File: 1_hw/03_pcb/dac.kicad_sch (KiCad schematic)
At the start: 6 parts, among them U16 AD9850, U17 AD9744

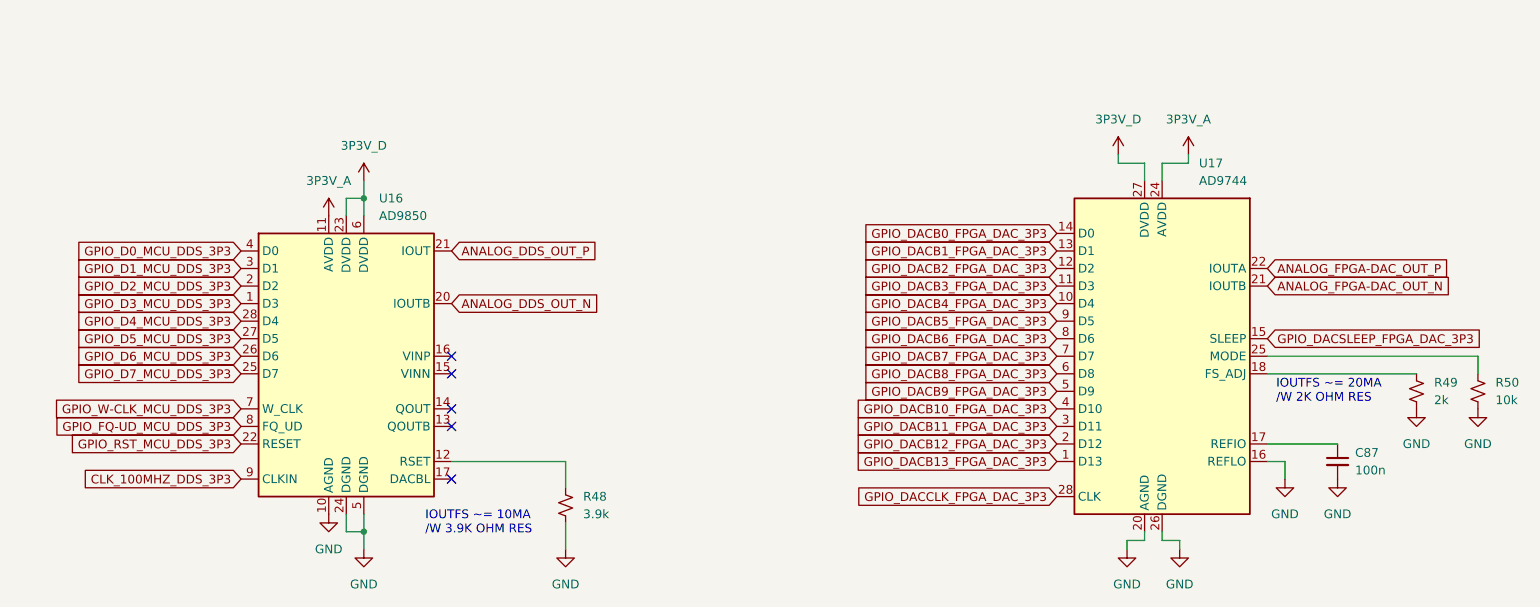
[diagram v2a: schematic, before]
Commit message: FEAT: Added MCU Flash. Finished creating & assigning footprints. Ran ERC & cleared out issues. Ready for Layout.
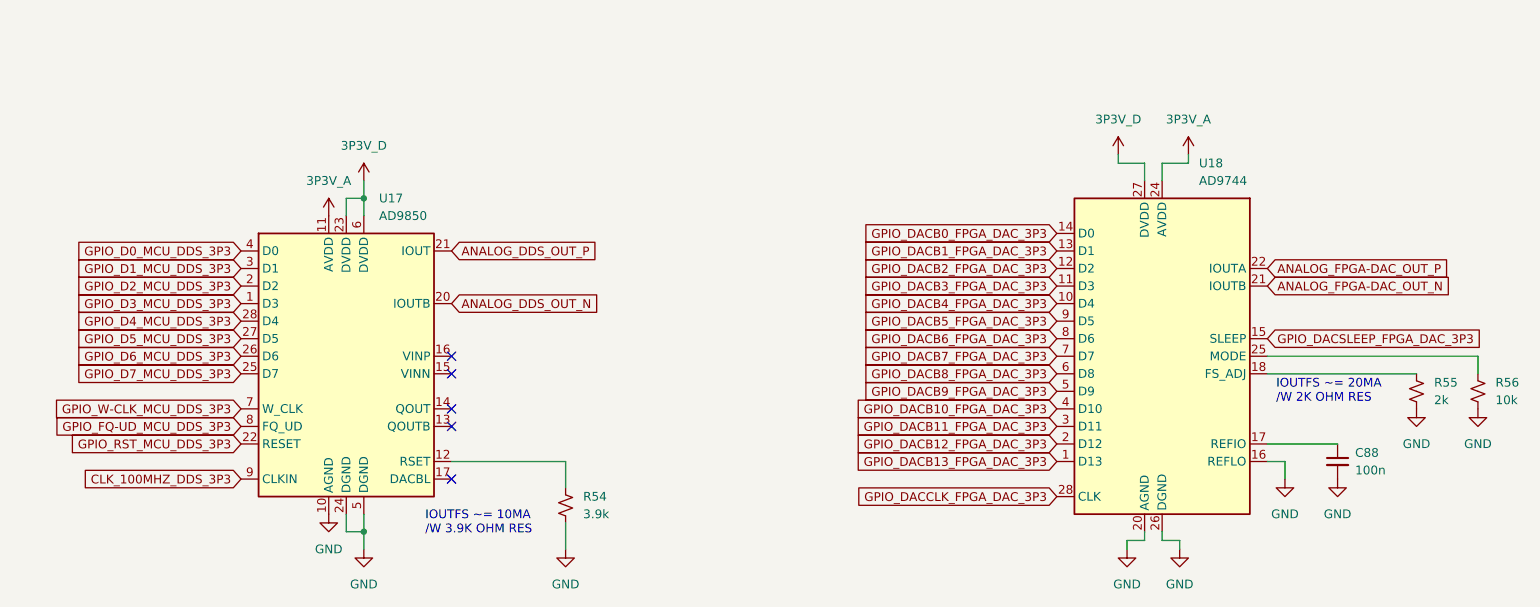
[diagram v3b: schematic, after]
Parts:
- renumbered C87 to C88, R48 to R54, R49 to R55, R50 to R56, U16 to U17, U17 to U18
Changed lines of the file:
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@@
 		(dnp no)
 		(fields_autoplaced yes)
-		(property "Reference" "#PWR0202"
+		(property "Reference" "#PWR0217"
 			(at 204.47 120.65 0)
 			(effects
@@
 			(project "arb"
 				(path "/866ef9be-3b01-4288-a6e0-a2357aa17e50/7126ceca-2dec-4994-855f-f217c0acdc71"
-					(reference "#PWR0202")
+					(reference "#PWR0217")
 					(unit 1)
 				)
@@
 		(dnp no)
 		(fields_autoplaced yes)
-		(property "Reference" "#PWR0206"
+		(property "Reference" "#PWR0221"
 			(at 234.95 110.49 0)
 			(effects
@@
 			(project "arb"
 				(path "/866ef9be-3b01-4288-a6e0-a2357aa17e50/7126ceca-2dec-4994-855f-f217c0acdc71"
-					(reference "#PWR0206")
+					(reference "#PWR0221")
 					(unit 1)
 				)
@@
 		(dnp no)
 		(fields_autoplaced yes)
-		(property "Reference" "#PWR0203"
+		(property "Reference" "#PWR0218"
 			(at 212.09 120.65 0)
 			(effects
@@
 			(project "arb"
 				(path "/866ef9be-3b01-4288-a6e0-a2357aa17e50/7126ceca-2dec-4994-855f-f217c0acdc71"
-					(reference "#PWR0203")
+					(reference "#PWR0218")
 					(unit 1)
 				)
@@
 		(dnp no)
 		(fields_autoplaced yes)
-		(property "Reference" "U16"
+		(property "Reference" "U17"
 			(at 96.1741 63.5 0)
 			(effects
@@
 			(project ""
 				(path "/866ef9be-3b01-4288-a6e0-a2357aa17e50/7126ceca-2dec-4994-855f-f217c0acdc71"
-					(reference "U16")
+					(reference "U17")
 					(unit 1)
 				)
@@
 		(dnp no)
 		(fields_autoplaced yes)
-		(property "Reference" "#PWR0198"
+		(property "Reference" "#PWR0213"
 			(at 93.98 64.77 0)
 			(effects
@@
 			(project "arb"
 				(path "/866ef9be-3b01-4288-a6e0-a2357aa17e50/7126ceca-2dec-4994-855f-f217c0acdc71"
-					(reference "#PWR0198")
+					(reference "#PWR0213")
 					(unit 1)
 				)
@@
 		(dnp no)
 		(fields_autoplaced yes)
-		(property "Reference" "#PWR0200"
+		(property "Reference" "#PWR0215"
 			(at 123.19 120.65 0)
 			(effects
@@
 			(project "arb"
 				(path "/866ef9be-3b01-4288-a6e0-a2357aa17e50/7126ceca-2dec-4994-855f-f217c0acdc71"
-					(reference "#PWR0200")
+					(reference "#PWR0215")
 					(unit 1)
 				)
@@
 		(dnp no)
 		(fields_autoplaced yes)
-		(property "Reference" "R48"
+		(property "Reference" "R54"
 			(at 125.73 106.6799 0)
 			(effects
@@
 			(project "arb"
 				(path "/866ef9be-3b01-4288-a6e0-a2357aa17e50/7126ceca-2dec-4994-855f-f217c0acdc71"
-					(reference "R48")
+					(reference "R54")
 					(unit 1)
 				)
@@
 		(dnp no)
 		(fields_autoplaced yes)
-		(property "Reference" "R50"
+		(property "Reference" "R56"
 			(at 257.81 90.1699 0)
 			(effects
@@
 			(project "arb"
 				(path "/866ef9be-3b01-4288-a6e0-a2357aa17e50/7126ceca-2dec-4994-855f-f217c0acdc71"
-					(reference "R50")
+					(reference "R56")
 					(unit 1)
 				)
@@
 		(dnp no)
 		(fields_autoplaced yes)
-		(property "Reference" "#PWR0204"
+		(property "Reference" "#PWR0219"
 			(at 213.36 60.96 0)
 			(effects
@@
 			(project "arb"
 				(path "/866ef9be-3b01-4288-a6e0-a2357aa17e50/7126ceca-2dec-4994-855f-f217c0acdc71"
-					(reference "#PWR0204")
+					(reference "#PWR0219")
 					(unit 1)
 				)
@@
 		(dnp no)
 		(fields_autoplaced yes)
-		(property "Reference" "#PWR0199"
+		(property "Reference" "#PWR0214"
 			(at 93.98 120.65 0)
 			(effects
@@
 			(project "arb"
 				(path "/866ef9be-3b01-4288-a6e0-a2357aa17e50/7126ceca-2dec-4994-855f-f217c0acdc71"
-					(reference "#PWR0199")
+					(reference "#PWR0214")
 					(unit 1)
 				)
@@
 		(dnp no)
 		(fields_autoplaced yes)
-		(property "Reference" "#PWR0208"
+		(property "Reference" "#PWR0223"
 			(at 255.27 100.33 0)
 			(effects
@@
 			(project "arb"
 				(path "/866ef9be-3b01-4288-a6e0-a2357aa17e50/7126ceca-2dec-4994-855f-f217c0acdc71"
-					(reference "#PWR0208")
+					(reference "#PWR0223")
 					(unit 1)
 				)
@@
 		(dnp no)
 		(fields_autoplaced yes)
-		(property "Reference" "R49"
+		(property "Reference" "R55"
 			(at 248.92 90.1699 0)
 			(effects
@@
 			(project "arb"
 				(path "/866ef9be-3b01-4288-a6e0-a2357aa17e50/7126ceca-2dec-4994-855f-f217c0acdc71"
-					(reference "R49")
+					(reference "R55")
 					(unit 1)
 				)
@@
 		(dnp no)
 		(fields_autoplaced yes)
-		(property "Reference" "#PWR0196"
+		(property "Reference" "#PWR0211"
 			(at 88.9 69.85 0)
 			(effects
@@
 			(project "arb"
 				(path "/866ef9be-3b01-4288-a6e0-a2357aa17e50/7126ceca-2dec-4994-855f-f217c0acdc71"
-					(reference "#PWR0196")
+					(reference "#PWR0211")
 					(unit 1)
 				)
@@
 		(dnp no)
 		(fields_autoplaced yes)
-		(property "Reference" "#PWR0201"
+		(property "Reference" "#PWR0216"
 			(at 203.2 60.96 0)
 			(effects
@@
 			(project "arb"
 				(path "/866ef9be-3b01-4288-a6e0-a2357aa17e50/7126ceca-2dec-4994-855f-f217c0acdc71"
-					(reference "#PWR0201")
+					(reference "#PWR0216")
 					(unit 1)
 				)
@@
 		(dnp no)
 		(fields_autoplaced yes)
-		(property "Reference" "#PWR0207"
+		(property "Reference" "#PWR0222"
 			(at 246.38 100.33 0)
 			(effects
@@
 			(project "arb"
 				(path "/866ef9be-3b01-4288-a6e0-a2357aa17e50/7126ceca-2dec-4994-855f-f217c0acdc71"
-					(reference "#PWR0207")
+					(reference "#PWR0222")
 					(unit 1)
 				)
@@
 		(dnp no)
 		(fields_autoplaced yes)
-		(property "Reference" "#PWR0197"
+		(property "Reference" "#PWR0212"
 			(at 88.9 115.57 0)
 			(effects
@@
 			(project "arb"
 				(path "/866ef9be-3b01-4288-a6e0-a2357aa17e50/7126ceca-2dec-4994-855f-f217c0acdc71"
-					(reference "#PWR0197")
+					(reference "#PWR0212")
 					(unit 1)
 				)
@@
 		(dnp no)
 		(fields_autoplaced yes)
-		(property "Reference" "#PWR0205"
+		(property "Reference" "#PWR0220"
 			(at 227.33 110.49 0)
 			(effects
@@
 			(project "arb"
 				(path "/866ef9be-3b01-4288-a6e0-a2357aa17e50/7126ceca-2dec-4994-855f-f217c0acdc71"
-					(reference "#PWR0205")
+					(reference "#PWR0220")
 					(unit 1)
 				)
@@
 		(dnp no)
 		(fields_autoplaced yes)
-		(property "Reference" "C87"
+		(property "Reference" "C88"
 			(at 237.49 100.3363 0)
 			(effects
@@
 			(project "arb"
 				(path "/866ef9be-3b01-4288-a6e0-a2357aa17e50/7126ceca-2dec-4994-855f-f217c0acdc71"
-					(reference "C87")
+					(reference "C88")
 					(unit 1)
 				)
@@
 		(on_board yes)
 		(dnp no)
-		(property "Reference" "U17"
+		(property "Reference" "U18"
 			(at 214.884 58.42 0)
 			(effects
@@
 			(project ""
 				(path "/866ef9be-3b01-4288-a6e0-a2357aa17e50/7126ceca-2dec-4994-855f-f217c0acdc71"
-					(reference "U17")
-					(unit 1)
-				)
+					(reference "U18")
+					(unit 1)
+				)

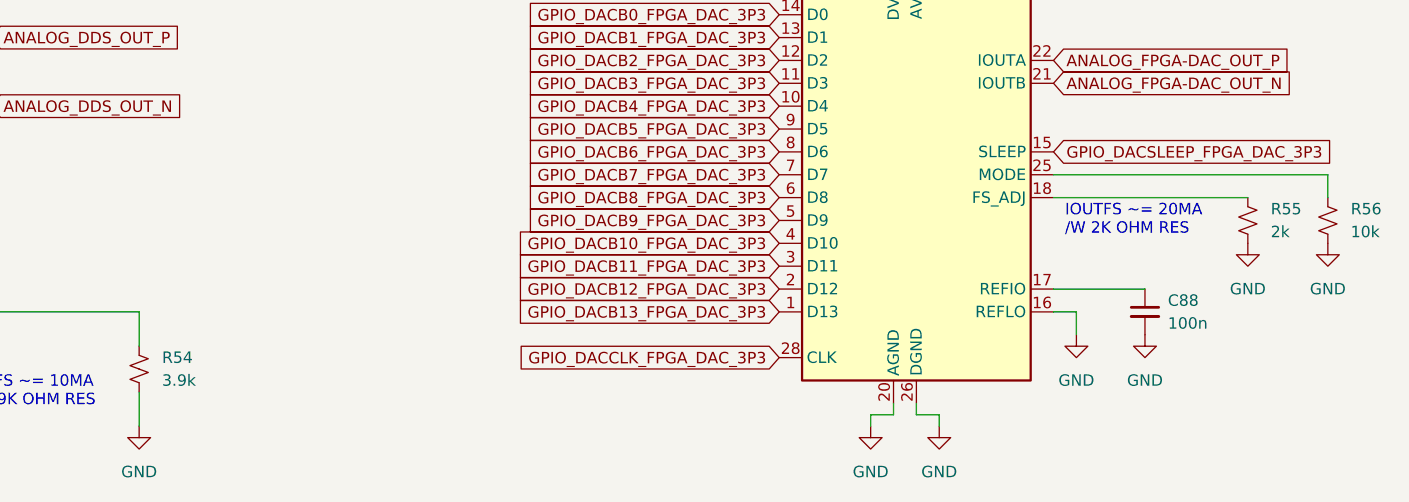
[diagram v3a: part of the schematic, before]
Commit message: MINOR: Verified Footprints to Datasheets. Added Pull Ups on FPGA DONE/Config/SPI Chip Select Pins.
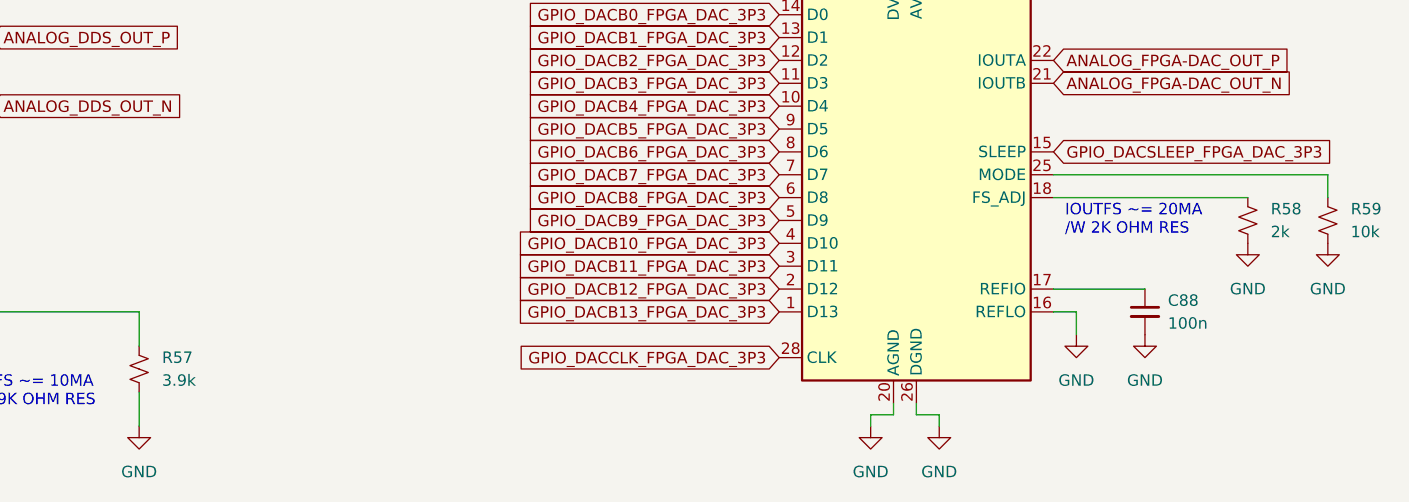
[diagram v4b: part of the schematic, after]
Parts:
- renumbered R54 to R57, R55 to R58, R56 to R59
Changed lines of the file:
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@@
 		(dnp no)
 		(fields_autoplaced yes)
-		(property "Reference" "#PWR0217"
+		(property "Reference" "#PWR0220"
 			(at 204.47 120.65 0)
 			(effects
@@
 			(project "arb"
 				(path "/866ef9be-3b01-4288-a6e0-a2357aa17e50/7126ceca-2dec-4994-855f-f217c0acdc71"
-					(reference "#PWR0217")
+					(reference "#PWR0220")
 					(unit 1)
 				)
@@
 		(dnp no)
 		(fields_autoplaced yes)
-		(property "Reference" "#PWR0221"
+		(property "Reference" "#PWR0224"
 			(at 234.95 110.49 0)
 			(effects
@@
 			(project "arb"
 				(path "/866ef9be-3b01-4288-a6e0-a2357aa17e50/7126ceca-2dec-4994-855f-f217c0acdc71"
-					(reference "#PWR0221")
+					(reference "#PWR0224")
 					(unit 1)
 				)
@@
 		(dnp no)
 		(fields_autoplaced yes)
-		(property "Reference" "#PWR0218"
+		(property "Reference" "#PWR0221"
 			(at 212.09 120.65 0)
 			(effects
@@
 			(project "arb"
 				(path "/866ef9be-3b01-4288-a6e0-a2357aa17e50/7126ceca-2dec-4994-855f-f217c0acdc71"
-					(reference "#PWR0218")
+					(reference "#PWR0221")
 					(unit 1)
 				)
@@
 		(dnp no)
 		(fields_autoplaced yes)
-		(property "Reference" "#PWR0213"
+		(property "Reference" "#PWR0216"
 			(at 93.98 64.77 0)
 			(effects
@@
 			(project "arb"
 				(path "/866ef9be-3b01-4288-a6e0-a2357aa17e50/7126ceca-2dec-4994-855f-f217c0acdc71"
-					(reference "#PWR0213")
+					(reference "#PWR0216")
 					(unit 1)
 				)
@@
 		(dnp no)
 		(fields_autoplaced yes)
-		(property "Reference" "#PWR0215"
+		(property "Reference" "#PWR0218"
 			(at 123.19 120.65 0)
 			(effects
@@
 			(project "arb"
 				(path "/866ef9be-3b01-4288-a6e0-a2357aa17e50/7126ceca-2dec-4994-855f-f217c0acdc71"
-					(reference "#PWR0215")
+					(reference "#PWR0218")
 					(unit 1)
 				)
@@
 		(dnp no)
 		(fields_autoplaced yes)
-		(property "Reference" "R54"
+		(property "Reference" "R57"
 			(at 125.73 106.6799 0)
 			(effects
@@
 			(project "arb"
 				(path "/866ef9be-3b01-4288-a6e0-a2357aa17e50/7126ceca-2dec-4994-855f-f217c0acdc71"
-					(reference "R54")
+					(reference "R57")
 					(unit 1)
 				)
@@
 		(dnp no)
 		(fields_autoplaced yes)
-		(property "Reference" "R56"
+		(property "Reference" "R59"
 			(at 257.81 90.1699 0)
 			(effects
@@
 			(project "arb"
 				(path "/866ef9be-3b01-4288-a6e0-a2357aa17e50/7126ceca-2dec-4994-855f-f217c0acdc71"
-					(reference "R56")
+					(reference "R59")
 					(unit 1)
 				)
@@
 		(dnp no)
 		(fields_autoplaced yes)
-		(property "Reference" "#PWR0219"
+		(property "Reference" "#PWR0222"
 			(at 213.36 60.96 0)
 			(effects
@@
 			(project "arb"
 				(path "/866ef9be-3b01-4288-a6e0-a2357aa17e50/7126ceca-2dec-4994-855f-f217c0acdc71"
-					(reference "#PWR0219")
+					(reference "#PWR0222")
 					(unit 1)
 				)
@@
 		(dnp no)
 		(fields_autoplaced yes)
-		(property "Reference" "#PWR0214"
+		(property "Reference" "#PWR0217"
 			(at 93.98 120.65 0)
 			(effects
@@
 			(project "arb"
 				(path "/866ef9be-3b01-4288-a6e0-a2357aa17e50/7126ceca-2dec-4994-855f-f217c0acdc71"
-					(reference "#PWR0214")
+					(reference "#PWR0217")
 					(unit 1)
 				)
@@
 		(dnp no)
 		(fields_autoplaced yes)
-		(property "Reference" "#PWR0223"
+		(property "Reference" "#PWR0226"
 			(at 255.27 100.33 0)
 			(effects
@@
 			(project "arb"
 				(path "/866ef9be-3b01-4288-a6e0-a2357aa17e50/7126ceca-2dec-4994-855f-f217c0acdc71"
-					(reference "#PWR0223")
+					(reference "#PWR0226")
 					(unit 1)
 				)
@@
 		(dnp no)
 		(fields_autoplaced yes)
-		(property "Reference" "R55"
+		(property "Reference" "R58"
 			(at 248.92 90.1699 0)
 			(effects
@@
 			(project "arb"
 				(path "/866ef9be-3b01-4288-a6e0-a2357aa17e50/7126ceca-2dec-4994-855f-f217c0acdc71"
-					(reference "R55")
+					(reference "R58")
 					(unit 1)
 				)
@@
 		(dnp no)
 		(fields_autoplaced yes)
-		(property "Reference" "#PWR0211"
+		(property "Reference" "#PWR0214"
 			(at 88.9 69.85 0)
 			(effects
@@
 			(project "arb"
 				(path "/866ef9be-3b01-4288-a6e0-a2357aa17e50/7126ceca-2dec-4994-855f-f217c0acdc71"
-					(reference "#PWR0211")
+					(reference "#PWR0214")
 					(unit 1)
 				)
@@
 		(dnp no)
 		(fields_autoplaced yes)
-		(property "Reference" "#PWR0216"
+		(property "Reference" "#PWR0219"
 			(at 203.2 60.96 0)
 			(effects
@@
 			(project "arb"
 				(path "/866ef9be-3b01-4288-a6e0-a2357aa17e50/7126ceca-2dec-4994-855f-f217c0acdc71"
-					(reference "#PWR0216")
+					(reference "#PWR0219")
 					(unit 1)
 				)
@@
 		(dnp no)
 		(fields_autoplaced yes)
-		(property "Reference" "#PWR0222"
+		(property "Reference" "#PWR0225"
 			(at 246.38 100.33 0)
 			(effects
@@
 			(project "arb"
 				(path "/866ef9be-3b01-4288-a6e0-a2357aa17e50/7126ceca-2dec-4994-855f-f217c0acdc71"
-					(reference "#PWR0222")
+					(reference "#PWR0225")
 					(unit 1)
 				)
@@
 		(dnp no)
 		(fields_autoplaced yes)
-		(property "Reference" "#PWR0212"
+		(property "Reference" "#PWR0215"
 			(at 88.9 115.57 0)
 			(effects
@@
 			(project "arb"
 				(path "/866ef9be-3b01-4288-a6e0-a2357aa17e50/7126ceca-2dec-4994-855f-f217c0acdc71"
-					(reference "#PWR0212")
+					(reference "#PWR0215")
 					(unit 1)
 				)
@@
 		(dnp no)
 		(fields_autoplaced yes)
-		(property "Reference" "#PWR0220"
+		(property "Reference" "#PWR0223"
 			(at 227.33 110.49 0)
 			(effects
@@
 			(project "arb"
 				(path "/866ef9be-3b01-4288-a6e0-a2357aa17e50/7126ceca-2dec-4994-855f-f217c0acdc71"
-					(reference "#PWR0220")
-					(unit 1)
-				)
+					(reference "#PWR0223")
+					(unit 1)
+				)
